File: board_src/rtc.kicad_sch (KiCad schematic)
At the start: 7 parts, among them IC1 PCF8563TS_4,118, J10 Conn_01x02_Pin, J9 Conn_01x02_Pin, Y2 Crystal

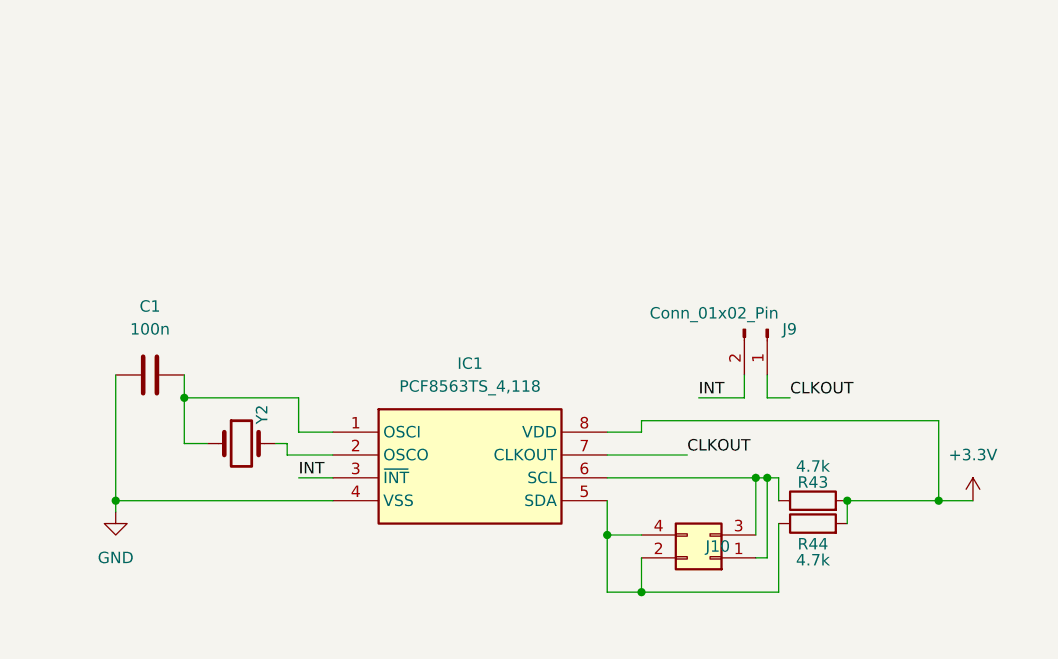
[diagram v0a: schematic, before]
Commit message: Poprawki w schematach. Rozpoczęte korekty płytki
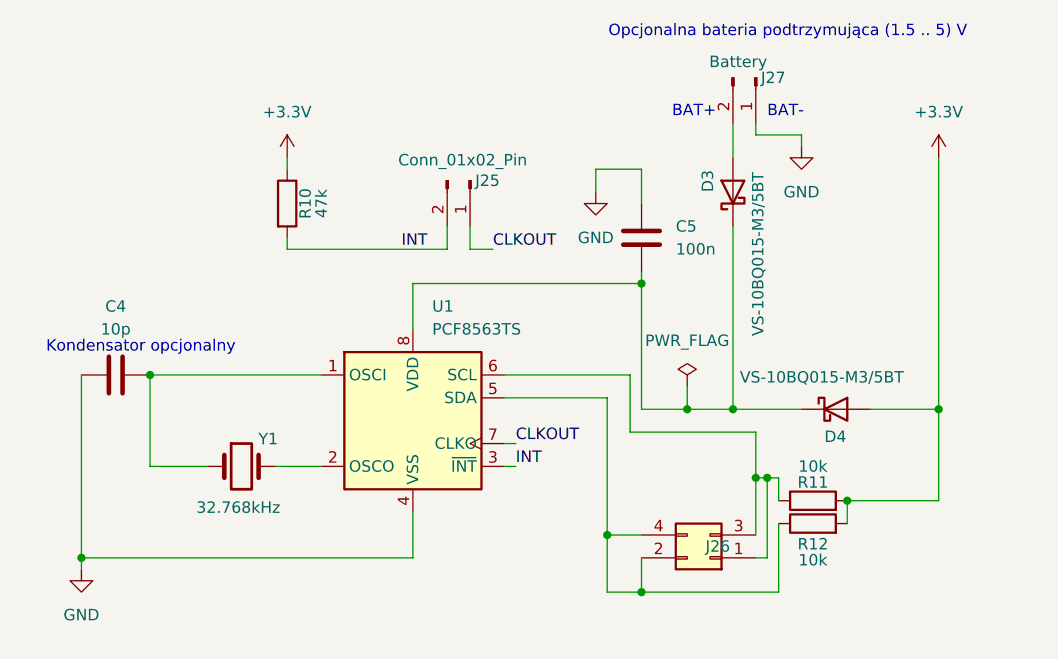
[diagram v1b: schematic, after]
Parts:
- removed IC1: PCF8563TS_4,118, footprints:SOP65P490X110-8N, symbol PCF8563TS_4_118:PCF8563TS_4,118
- added C5: 100n, Capacitor_SMD:C_0603_1608Metric_Pad1.08x0.95mm_HandSolder, symbol Device:C
- added D3: VS-10BQ015-M3/5BT, Diode_SMD:D_SMB_Handsoldering, symbol Device:D_Schottky
- added D4: VS-10BQ015-M3/5BT, Diode_SMD:D_SOD-123F, symbol Device:D_Schottky
- added J27: Battery, Connector_PinSocket_2.54mm:PinSocket_1x20_P2.54mm_Vertical, symbol Connector:Conn_01x02_Pin
- added R10: 47k, Resistor_SMD:R_0603_1608Metric_Pad0.98x0.95mm_HandSolder, symbol Device:R
- added U1: PCF8563TS, Package_SO:TSSOP-8_3x3mm_P0.65mm, symbol Timer_RTC:PCF8563TS
- C4: renamed from C1; value 100n -> 10p; footprint Capacitor_SMD:C_0603_1608Metric -> Capacitor_SMD:C_0603_1608Metric_Pad1.08x0.95mm_HandSolder
- J25: renamed from J9; footprint Connector_PinHeader_2.54mm:PinHeader_1x02_P2.54mm_Vertical -> Connector_PinHeader_2.54mm:PinHeader_1x04_P2.54mm_Vertical
- J26: renamed from J10; footprint Connector_PinHeader_2.54mm:PinHeader_2x02_P2.54mm_Vertical -> Connector_PinSocket_2.54mm:PinSocket_1x20_P2.54mm_Vertical
- R11: renamed from R43; value 4.7k -> 10k; footprint Resistor_SMD:R_0603_1608Metric -> Resistor_SMD:R_0603_1608Metric_Pad0.98x0.95mm_HandSolder
- R12: renamed from R44; value 4.7k -> 10k; footprint Resistor_SMD:R_0603_1608Metric -> Resistor_SMD:R_0603_1608Metric_Pad0.98x0.95mm_HandSolder
- Y1: renamed from Y2; value Crystal -> 32.768kHz
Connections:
- net +3.3V: now also D4.2 (A), R10.1
- net CLKOUT: now also U1.7 (CLKO)
- net GND: now also C5.2, J27.1 (Pin_1), U1.4 (VSS)
- net INT: now also R10.2, U1.3 (~{INT})
- net at J26.1 (Pin_1), J26.3 (Pin_3), R11.1: now also U1.6 (SCL)
- net at J26.2 (Pin_2), J26.4 (Pin_4), R12.1: now also U1.5 (SDA)
- net at C4.2, Y1.1: now also U1.1 (OSCI)
- net at Y1.2: now also U1.2 (OSCO)
- new net: D3.2 (A), J27.2 (Pin_2)
- new net: C5.1, D3.1 (K), D4.1 (K), U1.8 (VDD)
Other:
- note added: "BAT+"
- note added: "BAT-"
- note added: "Kondensator opcjonalny"
- note added: "Opcjonalna bateria podtrzymująca (1.5 .. 5) V"
- moved on the sheet: C4, J25, Y1

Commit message: Naniesione poprawki na projekcie płytki. Wersja końcowa
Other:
- moved on the sheet: R12
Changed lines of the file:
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@@
 	)
 	(junction
-		(at 233.68 80.01)
+		(at 215.9 88.9)
 		(diameter 0)
 		(color 0 0 0 0)
@@
 	)
 	(junction
-		(at 217.17 86.36)
-		(diameter 0)
-		(color 0 0 0 0)
-	)
-	(junction
 		(at 220.98 58.42)
 		(diameter 0)
@@
 	)
 	(junction
-		(at 220.98 92.71)
-		(diameter 0)
-		(color 0 0 0 0)
-	)
-	(junction
-		(at 234.95 80.01)
+		(at 234.95 86.36)
 		(diameter 0)
 		(color 0 0 0 0)
@@
 	)
 	(junction
+		(at 215.9 86.36)
+		(diameter 0)
+		(color 0 0 0 0)
+	)
+	(junction
+		(at 234.95 83.82)
+		(diameter 0)
+		(color 0 0 0 0)
+	)
+	(junction
 		(at 226.06 72.39)
 		(diameter 0)
@@
 	(wire
 		(pts
-			(xy 217.17 71.12) (xy 217.17 86.36)
+			(xy 234.95 88.9) (xy 233.68 88.9)
 		)
 		(stroke
@@
 	(wire
 		(pts
-			(xy 219.71 68.58) (xy 205.74 68.58)
-		)
-		(stroke
-			(width 0)
-			(type default)
-		)
-	)
-	(wire
-		(pts
 			(xy 254 44.45) (xy 254 72.39)
 		)
@@
 	(wire
 		(pts
-			(xy 217.17 92.71) (xy 220.98 92.71)
+			(xy 215.9 71.12) (xy 205.74 71.12)
 		)
 		(stroke
@@
 	(wire
 		(pts
-			(xy 234.95 88.9) (xy 234.95 80.01)
-		)
-		(stroke
-			(width 0)
-			(type default)
-		)
-	)
-	(wire
-		(pts
-			(xy 236.22 92.71) (xy 236.22 85.09)
-		)
-		(stroke
-			(width 0)
-			(type default)
-		)
-	)
-	(wire
-		(pts
 			(xy 215.9 45.72) (xy 215.9 48.26)
 		)
@@
 	(wire
 		(pts
-			(xy 243.84 82.55) (xy 243.84 85.09)
+			(xy 243.84 82.55) (xy 243.84 92.71)
 		)
 		(stroke
@@
 	(wire
 		(pts
-			(xy 219.71 74.93) (xy 219.71 68.58)
+			(xy 218.44 68.58) (xy 218.44 83.82)
 		)
 		(stroke
@@
 	(wire
 		(pts
-			(xy 233.68 80.01) (xy 233.68 74.93)
-		)
-		(stroke
-			(width 0)
-			(type default)
-		)
-	)
-	(wire
-		(pts
-			(xy 233.68 88.9) (xy 234.95 88.9)
-		)
-		(stroke
-			(width 0)
-			(type default)
-		)
-	)
-	(wire
-		(pts
-			(xy 233.68 80.01) (xy 233.68 86.36)
+			(xy 233.68 86.36) (xy 234.95 86.36)
 		)
 		(stroke
@@
 	(wire
 		(pts
-			(xy 234.95 80.01) (xy 236.22 80.01)
+			(xy 215.9 86.36) (xy 215.9 88.9)
+		)
+		(stroke
+			(width 0)
+			(type default)
+		)
+	)
+	(wire
+		(pts
+			(xy 215.9 92.71) (xy 215.9 88.9)
 		)
 		(stroke
@@
 	(wire
 		(pts
-			(xy 236.22 80.01) (xy 236.22 82.55)
+			(xy 234.95 86.36) (xy 234.95 88.9)
 		)
 		(stroke
@@
 	(wire
 		(pts
-			(xy 220.98 92.71) (xy 236.22 92.71)
-		)
-		(stroke
-			(width 0)
-			(type default)
-		)
-	)
-	(wire
-		(pts
-			(xy 220.98 88.9) (xy 220.98 92.71)
-		)
-		(stroke
-			(width 0)
-			(type default)
-		)
-	)
-	(wire
-		(pts
 			(xy 220.98 49.53) (xy 220.98 45.72)
 		)
@@
 	(wire
 		(pts
-			(xy 217.17 86.36) (xy 217.17 92.71)
+			(xy 218.44 68.58) (xy 205.74 68.58)
 		)
 		(stroke
@@
 	(wire
 		(pts
-			(xy 217.17 86.36) (xy 220.98 86.36)
-		)
-		(stroke
-			(width 0)
-			(type default)
-		)
-	)
-	(wire
-		(pts
 			(xy 231.14 52.07) (xy 231.14 72.39)
 		)
@@
 	(wire
 		(pts
-			(xy 233.68 80.01) (xy 234.95 80.01)
+			(xy 215.9 92.71) (xy 236.22 92.71)
+		)
+		(stroke
+			(width 0)
+			(type default)
+		)
+	)
+	(wire
+		(pts
+			(xy 215.9 88.9) (xy 220.98 88.9)
 		)
 		(stroke
@@
 	(wire
 		(pts
-			(xy 233.68 74.93) (xy 219.71 74.93)
+			(xy 234.95 83.82) (xy 234.95 86.36)
+		)
+		(stroke
+			(width 0)
+			(type default)
+		)
+	)
+	(wire
+		(pts
+			(xy 234.95 83.82) (xy 218.44 83.82)
+		)
+		(stroke
+			(width 0)
+			(type default)
+		)
+	)
+	(wire
+		(pts
+			(xy 236.22 82.55) (xy 234.95 82.55)
 		)
 		(stroke
@@
 	(wire
 		(pts
+			(xy 234.95 83.82) (xy 234.95 82.55)
+		)
+		(stroke
+			(width 0)
+			(type default)
+		)
+	)
+	(wire
+		(pts
 			(xy 199.39 52.07) (xy 199.39 54.61)
 		)
@@
 	(wire
 		(pts
-			(xy 217.17 71.12) (xy 205.74 71.12)
+			(xy 215.9 86.36) (xy 220.98 86.36)
 		)
 		(stroke
@@
 		(pts
 			(xy 166.37 68.58) (xy 185.42 68.58)
+		)
+		(stroke
+			(width 0)
+			(type default)
+		)
+	)
+	(wire
+		(pts
+			(xy 215.9 71.12) (xy 215.9 86.36)
 		)
 		(stroke
@@
 	(symbol
 		(lib_id "Device:R")
-		(at 240.03 85.09 90)
+		(at 240.03 92.71 90)
 		(unit 1)
 		(exclude_from_sim no)
@@
 		(dnp no)
 		(property "Reference" "R12"
-			(at 240.03 87.376 90)
+			(at 240.03 94.996 90)
 			(effects
 				(font
@@
 		)
 		(property "Value" "10k"
-			(at 240.03 89.154 90)
+			(at 240.03 96.774 90)
 			(effects
 				(font
@@
 		)
 		(property "Footprint" "Resistor_SMD:R_0603_1608Metric_Pad0.98x0.95mm_HandSolder"
-			(at 240.03 86.868 90)
+			(at 240.03 94.488 90)
 			(effects
 				(font
@@
 		)
 		(property "Datasheet" "~"
-			(at 240.03 85.09 0)
+			(at 240.03 92.71 0)
 			(effects
 				(font
@@
 		)
 		(property "Description" "Resistor"
-			(at 240.03 85.09 0)
-			(effects
-				(font
+			(at 240.03 92.71 0)
+			(effects
+				(font

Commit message: Wprowadzono usprawnienia i poprawki. Wersja ostateczna, wysłana do JLCPCB.
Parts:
- D4: footprint Diode_SMD:D_SOD-123F -> Diode_SMD:D_SMB_Handsoldering
- J25: footprint Connector_PinHeader_2.54mm:PinHeader_1x04_P2.54mm_Vertical -> Connector_PinHeader_2.54mm:PinHeader_1x02_P2.54mm_Vertical
- J26, J27: footprint Connector_PinSocket_2.54mm:PinSocket_1x20_P2.54mm_Vertical -> Connector_PinHeader_2.54mm:PinHeader_1x02_P2.54mm_Vertical
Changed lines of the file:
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@@
 			)
 		)
-		(property "Footprint" "Connector_PinSocket_2.54mm:PinSocket_1x20_P2.54mm_Vertical"
+		(property "Footprint" "Connector_PinHeader_2.54mm:PinHeader_1x02_P2.54mm_Vertical"
 			(at 228.6 88.9 0)
 			(effects
@@
 			)
 		)
-		(property "Footprint" "Connector_PinSocket_2.54mm:PinSocket_1x20_P2.54mm_Vertical"
+		(property "Footprint" "Connector_PinHeader_2.54mm:PinHeader_1x02_P2.54mm_Vertical"
 			(at 233.68 35.56 0)
 			(effects
@@
 			)
 		)
-		(property "Footprint" "Connector_PinHeader_2.54mm:PinHeader_1x04_P2.54mm_Vertical"
+		(property "Footprint" "Connector_PinHeader_2.54mm:PinHeader_1x02_P2.54mm_Vertical"
 			(at 201.93 46.99 0)
 			(effects
@@
 			)
 		)
-		(property "Footprint" "Diode_SMD:D_SOD-123F"
+		(property "Footprint" "Diode_SMD:D_SMB_Handsoldering"
 			(at 242.57 72.39 0)
 			(effects
